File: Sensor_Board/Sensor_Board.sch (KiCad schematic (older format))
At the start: 0 parts

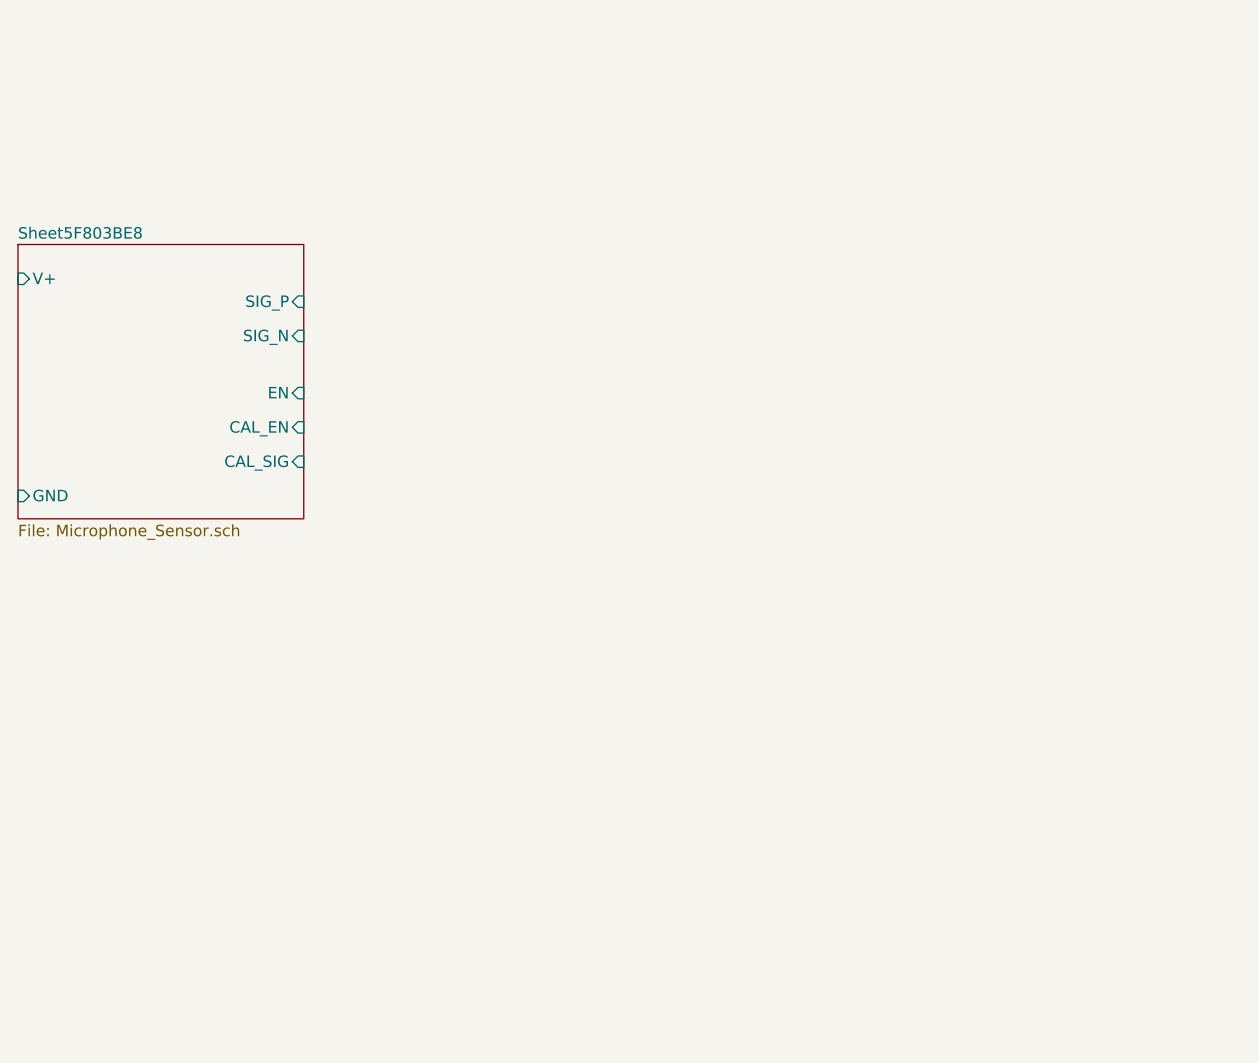
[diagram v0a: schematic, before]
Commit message: Add mic array
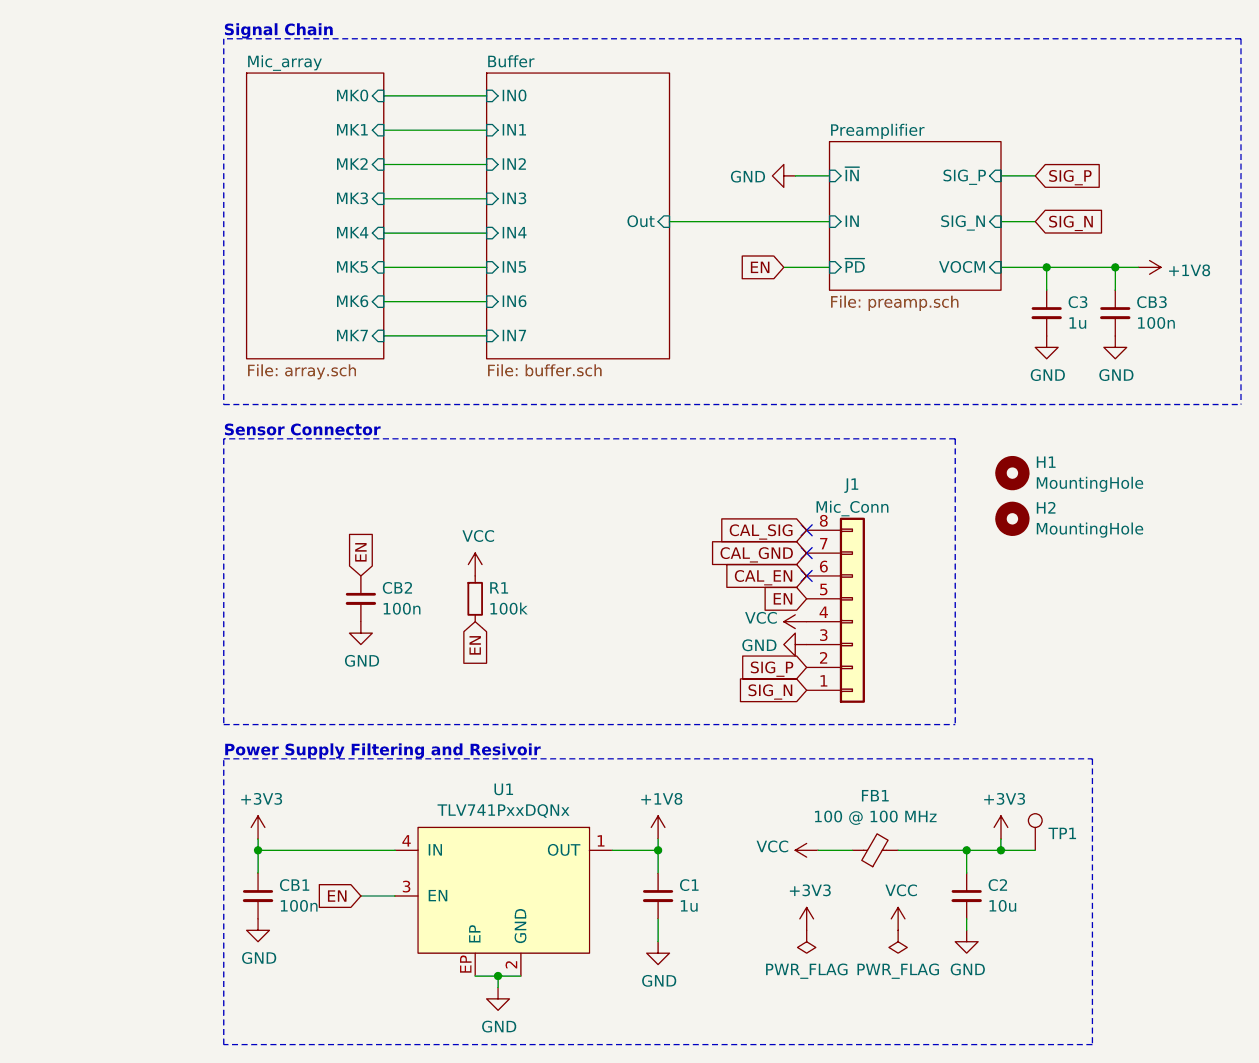
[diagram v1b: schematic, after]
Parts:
- added C1, C3: 1u, Capacitor_SMD:C_0603_1608Metric_Pad1.08x0.95mm_HandSolder, symbol Device:C_Small
- added C2: 10u, Capacitor_SMD:C_0603_1608Metric_Pad1.08x0.95mm_HandSolder, symbol Device:C_Small
- added CB1, CB2, CB3: 100n, Capacitor_SMD:C_0603_1608Metric_Pad1.08x0.95mm_HandSolder, symbol Device:C_Small
- added FB1: 100 @ 100 MHz, Inductor_SMD:L_0603_1608Metric_Pad1.05x0.95mm_HandSolder, symbol Device:Ferrite_Bead_Small
- added H1, H2: MountingHole, MountingHole:MountingHole_2.7mm_M2.5_DIN965_Pad, symbol Mechanical:MountingHole
- added J1: Mic_Conn, Connector_PinHeader_2.54mm:PinHeader_1x08_P2.54mm_Vertical, symbol Connector_Generic:Conn_01x08
- added R1: 100k, Resistor_SMD:R_0603_1608Metric_Pad0.98x0.95mm_HandSolder, symbol Device:R_Small
- added TP1: TestPoint, TestPoint:TestPoint_Pad_D1.0mm, symbol Connector:TestPoint
- added U1: TLV741PxxDQNx, symbol grootvoet:TLV741PxxDQNx
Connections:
- new net +1V8: C1.1, C3.1, CB3.1, U1.1 (OUT)
- new net +3V3: C2.1, CB1.1, FB1.2, TP1.1, U1.4 (IN)
- new net CAL_EN: J1.6 (Pin_6)
- new net CAL_GND: J1.7 (Pin_7)
- new net CAL_SIG: J1.8 (Pin_8)
- new net EN: CB2.1, J1.5 (Pin_5), R1.2, U1.3 (EN)
- new net GND: C1.2, C2.2, C3.2, CB1.2, CB2.2, CB3.2, J1.3 (Pin_3), U1.2 (GND), U1.EP
- new net SIG_N: J1.1 (Pin_1)
- new net SIG_P: J1.2 (Pin_2)
- new net VCC: FB1.1, J1.4 (Pin_4), R1.1
- no-connect marks 0 -> 3
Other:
- note added: "Power Supply Filtering and Resivoir"
- note added: "Sensor Connector"
- note added: "Signal Chain"

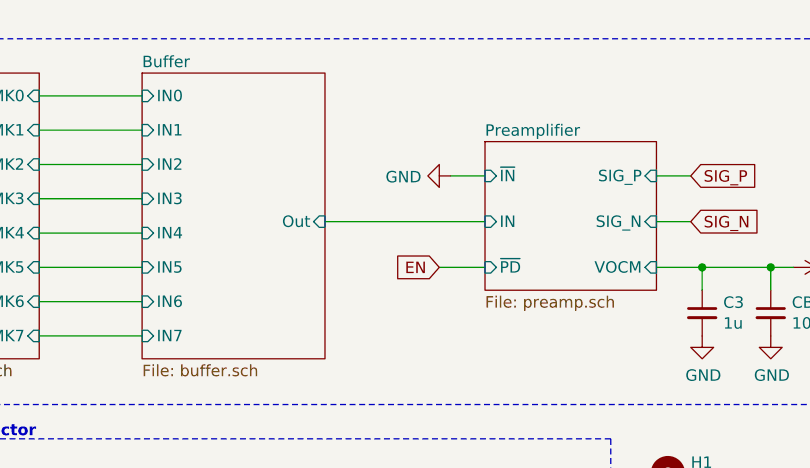
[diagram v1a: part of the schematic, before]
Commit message: Assign footprints
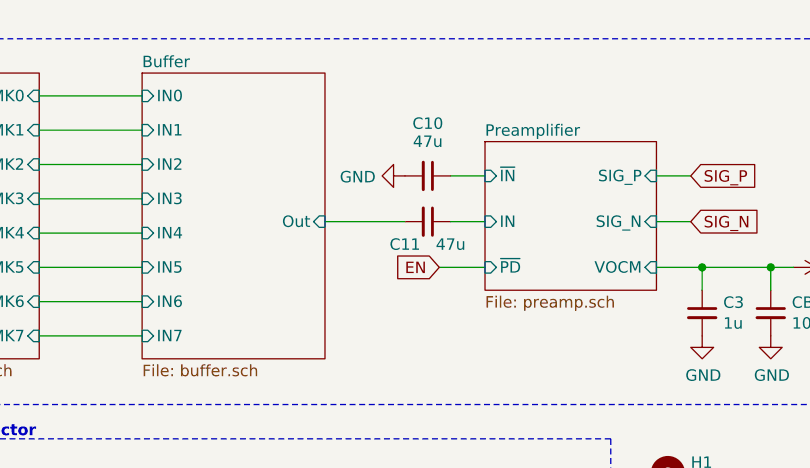
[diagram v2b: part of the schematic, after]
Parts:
- added C10, C11: 47u, Capacitor_SMD:C_1206_3216Metric_Pad1.33x1.80mm_HandSolder, symbol Device:C_Small
- C2: MPN (none) -> C0805C106K9PACTU
- U1: footprint (none) -> grootvoet:Texas_X2SON-4_1x1mm_P0.65mm; MFN (none) -> TLV74118PDQNR; Mfr. (none) -> TI
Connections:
- net Buffer/Out: now also C11.2
- net GND: now also C10.2
- new net Preamplifier/IN: C11.1
- new net Preamplifier/~IN: C10.1
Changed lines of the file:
@@
 AR Path="/5EE5ECAD/5F0090C7/5F976141" Ref="#FLG?"  Part="1"
 AR Path="/5F803BE9/5F976141" Ref="#FLG?"  Part="1"
-AR Path="/5F976141" Ref="#FLG0101"  Part="1"
-F 0 "#FLG0101" H 5600 5625 50  0001 C CNN
+AR Path="/5F976141" Ref="#FLG01"  Part="1"
+F 0 "#FLG01" H 5600 5625 50  0001 C CNN
 F 1 "PWR_FLAG" H 5600 5723 50  0000 C CNN
 F 2 "" H 5600 5550 50  0001 C CNN
@@
 F 2 "Capacitor_SMD:C_0603_1608Metric_Pad1.08x0.95mm_HandSolder" H 6300 5400 50  0001 C CNN
 F 3 "~" H 6300 5400 50  0001 C CNN
-F 4 "" H 6300 5400 50  0001 C CNN "MPN"
+F 4 "C0805C106K9PACTU" H 6300 5400 50  0001 C CNN "MPN"
 F 5 "KEMET" H 6300 5400 50  0001 C CNN "Mfr."
 	1    6300 5400
@@
 F 0 "U1" H 4275 5665 50  0000 C CNN
 F 1 "TLV741PxxDQNx" H 4275 5574 50  0000 C CNN
-F 2 "" H 4650 4900 50  0001 C CNN
+F 2 "grootvoet:Texas_X2SON-4_1x1mm_P0.65mm" H 4650 4900 50  0001 C CNN
 F 3 "" H 4650 4900 50  0001 C CNN
+F 4 "TLV74118PDQNR" H 4250 5300 50  0001 C CNN "MFN"
+F 5 "TI" H 4250 5300 50  0001 C CNN "Mfr."
 	1    4250 5300
 	1    0    0    -1
 $EndComp
 $Comp
-L power:VCC #PWR0101
+L power:VCC #PWR012
 U 1 1 5F9B0A7B
 P 5650 5200
-F 0 "#PWR0101" H 5650 5050 50  0001 C CNN
+F 0 "#PWR012" H 5650 5050 50  0001 C CNN
 F 1 "VCC" V 5665 5327 50  0000 L CNN
 F 2 "" H 5650 5200 50  0001 C CNN
@@
 $EndComp
 $Comp
-L power:+3V3 #PWR0102
+L power:+3V3 #PWR015
 U 1 1 5F9B1220
 P 6450 5150
-F 0 "#PWR0102" H 6450 5000 50  0001 C CNN
+F 0 "#PWR015" H 6450 5000 50  0001 C CNN
 F 1 "+3V3" H 6465 5323 50  0000 C CNN
 F 2 "" H 6450 5150 50  0001 C CNN
@@
 $EndComp
 $Comp
-L power:+3V3 #PWR0103
+L power:+3V3 #PWR011
 U 1 1 5F9BEFD6
 P 5600 5550
-F 0 "#PWR0103" H 5600 5400 50  0001 C CNN
+F 0 "#PWR011" H 5600 5400 50  0001 C CNN
 F 1 "+3V3" H 5615 5723 50  0000 C CNN
 F 2 "" H 5600 5550 50  0001 C CNN
@@
 AR Path="/5EE5ECAD/5F0090C7/5F9BFE28" Ref="#FLG?"  Part="1"
 AR Path="/5F803BE9/5F9BFE28" Ref="#FLG?"  Part="1"
-AR Path="/5F9BFE28" Ref="#FLG0102"  Part="1"
-F 0 "#FLG0102" H 6000 5625 50  0001 C CNN
+AR Path="/5F9BFE28" Ref="#FLG02"  Part="1"
+F 0 "#FLG02" H 6000 5625 50  0001 C CNN
 F 1 "PWR_FLAG" H 6000 5723 50  0000 C CNN
 F 2 "" H 6000 5550 50  0001 C CNN
@@
 $EndComp
 $Comp
-L power:VCC #PWR0104
+L power:VCC #PWR013
 U 1 1 5F9C2F1F
 P 6000 5550
-F 0 "#PWR0104" H 6000 5400 50  0001 C CNN
+F 0 "#PWR013" H 6000 5400 50  0001 C CNN
 F 1 "VCC" H 6015 5723 50  0000 C CNN
 F 2 "" H 6000 5550 50  0001 C CNN
@@
 F7 "VOCM" I R 6450 2650 50
 $EndSheet
-Wire Wire Line
-	5700 2450 5000 2450
-$Comp
-L power:GND #PWR0105
+$Comp
+L power:GND #PWR08
 U 1 1 5FA16F62
-P 5550 2250
-F 0 "#PWR0105" H 5550 2000 50  0001 C CNN
-F 1 "GND" V 5555 2122 50  0000 R CNN
-F 2 "" H 5550 2250 50  0001 C CNN
-F 3 "" H 5550 2250 50  0001 C CNN
-	1    5550 2250
+P 5350 2250
+F 0 "#PWR08" H 5350 2000 50  0001 C CNN
+F 1 "GND" V 5355 2122 50  0000 R CNN
+F 2 "" H 5350 2250 50  0001 C CNN
+F 3 "" H 5350 2250 50  0001 C CNN
+	1    5350 2250
 	0    1    1    0
 $EndComp
@@
 $EndComp
 $Comp
-L power:GND #PWR0106
+L power:GND #PWR07
 U 1 1 5FA1DA82
 P 4950 5600
-F 0 "#PWR0106" H 4950 5350 50  0001 C CNN
+F 0 "#PWR07" H 4950 5350 50  0001 C CNN
 F 1 "GND" H 4955 5427 50  0000 C CNN
 F 2 "" H 4950 5600 50  0001 C CNN
@@
 	4950 5600 4950 5500
 $Comp
-L power:GND #PWR0107
+L power:GND #PWR05
 U 1 1 5FA1E710
 P 4250 5800
-F 0 "#PWR0107" H 4250 5550 50  0001 C CNN
+F 0 "#PWR05" H 4250 5550 50  0001 C CNN
 F 1 "GND" H 4255 5627 50  0000 C CNN
 F 2 "" H 4250 5800 50  0001 C CNN
@@
 SIG_N
 $Comp
-L power:VCC #PWR0108
+L power:VCC #PWR09
 U 1 1 5FA24F87
 P 5600 4200
-F 0 "#PWR0108" H 5600 4050 50  0001 C CNN
+F 0 "#PWR09" H 5600 4050 50  0001 C CNN
 F 1 "VCC" V 5615 4327 50  0000 L CNN
 F 2 "" H 5600 4200 50  0001 C CNN
@@
 $EndComp
 $Comp
-L power:GND #PWR0109
+L power:GND #PWR010
 U 1 1 5FA257DC
 P 5600 4300
-F 0 "#PWR0109" H 5600 4050 50  0001 C CNN
+F 0 "#PWR010" H 5600 4050 50  0001 C CNN
 F 1 "GND" V 5605 4172 50  0000 R CNN
 F 2 "" H 5600 4300 50  0001 C CNN
@@
 $EndComp
 $Comp
-L power:GND #PWR0110
+L power:GND #PWR03
 U 1 1 5FA272C8
 P 3650 4200
-F 0 "#PWR0110" H 3650 3950 50  0001 C CNN
+F 0 "#PWR03" H 3650 3950 50  0001 C CNN
 F 1 "GND" H 3655 4027 50  0000 C CNN
 F 2 "" H 3650 4200 50  0001 C CNN
@@
 EN
 $Comp
-L power:GND #PWR0111
+L power:GND #PWR014
 U 1 1 5FA28A18
 P 6300 5550
-F 0 "#PWR0111" H 6300 5300 50  0001 C CNN
+F 0 "#PWR014" H 6300 5300 50  0001 C CNN
 F 1 "GND" H 6305 5377 50  0000 C CNN
 F 2 "" H 6300 5550 50  0001 C CNN
@@
 $EndComp
 $Comp
-L power:GND #PWR0112
+L power:GND #PWR02
 U 1 1 5FA368EF
 P 3200 5500
-AR Path="/5FA368EF" Ref="#PWR0112"  Part="1"
+AR Path="/5FA368EF" Ref="#PWR02"  Part="1"
 AR Path="/5F9C4001/5FA368EF" Ref="#PWR?"  Part="1"
-F 0 "#PWR0112" H 3200 5250 50  0001 C CNN
+F 0 "#PWR02" H 3200 5250 50  0001 C CNN
 F 1 "GND" H 3205 5327 50  0000 C CNN
 F 2 "" H 3200 5500 50  0001 C CNN
@@
 Connection ~ 3200 5200
 $Comp
-L power:+1V8 #PWR0113
+L power:+1V8 #PWR06
 U 1 1 5FA3AC62
 P 4950 5150
-F 0 "#PWR0113" H 4950 5000 50  0001 C CNN
+F 0 "#PWR06" H 4950 5000 50  0001 C CNN
 F 1 "+1V8" H 4965 5323 50  0000 C CNN
 F 2 "" H 4950 5150 50  0001 C CNN
@@
 SIG_N
 $Comp
-L power:+1V8 #PWR0114
+L power:+1V8 #PWR018
 U 1 1 5FA58879
 P 7050 2650
-F 0 "#PWR0114" H 7050 2500 50  0001 C CNN
+F 0 "#PWR018" H 7050 2500 50  0001 C CNN
 F 1 "+1V8" V 7065 2778 50  0000 L CNN
 F 2 "" H 7050 2650 50  0001 C CNN
@@
 $EndComp
 $Comp
-L power:GND #PWR0115
+L power:GND #PWR016
 U 1 1 5FA5C984
 P 6650 2950
-F 0 "#PWR0115" H 6650 2700 50  0001 C CNN
+F 0 "#PWR016" H 6650 2700 50  0001 C CNN
 F 1 "GND" H 6655 2777 50  0000 C CNN
 F 2 "" H 6650 2950 50  0001 C CNN
@@
 	6950 2650 6650 2650
 $Comp
-L power:GND #PWR0116
+L power:GND #PWR017
 U 1 1 5FA5F877
 P 6950 2950
-F 0 "#PWR0116" H 6950 2700 50  0001 C CNN
+F 0 "#PWR017" H 6950 2700 50  0001 C CNN
 F 1 "GND" H 6955 2777 50  0000 C CNN
 F 2 "" H 6950 2950 50  0001 C CNN
@@
 $EndComp
 $Comp
-L power:VCC #PWR0117
+L power:VCC #PWR04
 U 1 1 5FA6370F
 P 4150 4000
-F 0 "#PWR0117" H 4150 3850 50  0001 C CNN
+F 0 "#PWR04" H 4150 3850 50  0001 C CNN
 F 1 "VCC" H 4165 4173 50  0000 C CNN
 F 2 "" H 4150 4000 50  0001 C CNN
@@
 NoConn ~ 5600 3800
 $Comp
-L power:+3V3 #PWR0118
+L power:+3V3 #PWR01
 U 1 1 5FAA8260
 P 3200 5150
-F 0 "#PWR0118" H 3200 5000 50  0001 C CNN
+F 0 "#PWR01" H 3200 5000 50  0001 C CNN
 F 1 "+3V3" H 3215 5323 50  0000 C CNN
 F 2 "" H 3200 5150 50  0001 C CNN
@@
 Text GLabel 5500 2650 0    50   Input ~ 0
 EN
+$Comp
+L Device:C_Small C?
+U 1 1 5FAC4E7D
+P 5450 2250
+AR Path="/5EE5ECAD/5EECE6B8/5FAC4E7D" Ref="C?"  Part="1"
+AR Path="/5EE5ECAD/5EF21991/5FAC4E7D" Ref="C?"  Part="1"
+AR Path="/5EE5ECAD/5EF33EA2/5FAC4E7D" Ref="C?"  Part="1"
+AR Path="/5EE5ECAD/5EF4C631/5FAC4E7D" Ref="C?"  Part="1"
+AR Path="/5EE5ECAD/5F0013E5/5FAC4E7D" Ref="C?"  Part="1"
+AR Path="/5EE5ECAD/5F0090C7/5FAC4E7D" Ref="C?"  Part="1"
+AR Path="/5F803BE9/5FAC4E7D" Ref="C?"  Part="1"
+AR Path="/5FAC4E7D" Ref="C10"  Part="1"
+AR Path="/5F9C4001/5FAC4E7D" Ref="C?"  Part="1"
+F 0 "C10" V 5221 2250 50  0000 C CNN
+F 1 "47u" V 5300 2250 50  0000 C CNN
+F 2 "Capacitor_SMD:C_1206_3216Metric_Pad1.33x1.80mm_HandSolder" H 5450 2250 50  0001 C CNN
+F 3 "~" H 5450 2250 50  0001 C CNN
+F 4 "GRM31CR60J107KE39K" V 5450 2250 50  0001 C CNN "MPN"
+F 5 "Murata Electronics" V 5450 2250 50  0001 C CNN "Mfr."
+F 6 "Specified 47u but that is min. (>47u is better)" V 5450 2250 50  0001 C CNN "Notes"
+	1    5450 2250
+	0    1    1    0
+$EndComp
+$Comp
+L Device:C_Small C?
+U 1 1 5FAC7016
+P 5450 2450
+AR Path="/5EE5ECAD/5EECE6B8/5FAC7016" Ref="C?"  Part="1"
+AR Path="/5EE5ECAD/5EF21991/5FAC7016" Ref="C?"  Part="1"
+AR Path="/5EE5ECAD/5EF33EA2/5FAC7016" Ref="C?"  Part="1"
+AR Path="/5EE5ECAD/5EF4C631/5FAC7016" Ref="C?"  Part="1"
+AR Path="/5EE5ECAD/5F0013E5/5FAC7016" Ref="C?"  Part="1"
+AR Path="/5EE5ECAD/5F0090C7/5FAC7016" Ref="C?"  Part="1"
+AR Path="/5F803BE9/5FAC7016" Ref="C?"  Part="1"
+AR Path="/5FAC7016" Ref="C11"  Part="1"
+AR Path="/5F9C4001/5FAC7016" Ref="C?"  Part="1"
+F 0 "C11" V 5550 2350 50  0000 C CNN
+F 1 "47u" V 5550 2550 50  0000 C CNN
+F 2 "Capacitor_SMD:C_1206_3216Metric_Pad1.33x1.80mm_HandSolder" H 5450 2450 50  0001 C CNN
+F 3 "~" H 5450 2450 50  0001 C CNN
+F 4 "GRM31CR60J107KE39K" V 5450 2450 50  0001 C CNN "MPN"
+F 5 "Murata Electronics" V 5450 2450 50  0001 C CNN "Mfr."
+F 6 "Specified 47u but that is min. (>47u is better)" V 5450 2450 50  0001 C CNN "Notes"
+	1    5450 2450
+	0    1    1    0
+$EndComp
+Wire Wire Line
+	5550 2450 5700 2450
+Wire Wire Line
+	5350 2450 5000 2450
 $EndSCHEMATC
